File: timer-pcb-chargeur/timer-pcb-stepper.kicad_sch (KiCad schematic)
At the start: 7 parts, among them J11 JST_04, J3 On/off

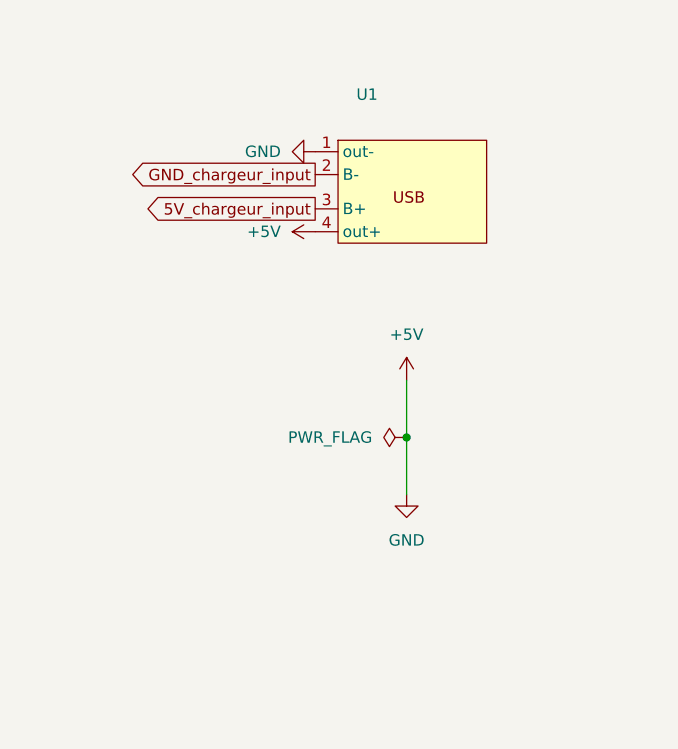
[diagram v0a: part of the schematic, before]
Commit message: mise à jour fichier kicad stepper + led. création dossier chargeur PCB.création du fichier .rpt
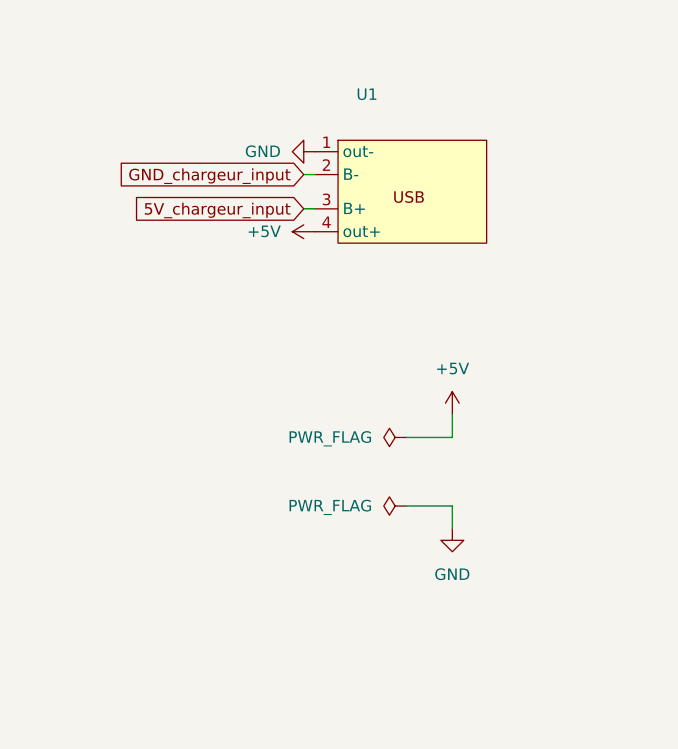
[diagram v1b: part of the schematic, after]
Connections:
- net +5V: no longer J11.1, U1.1 (out-)
- new net GND: J11.1, U1.1 (out-)
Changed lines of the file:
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@@
 		(date "27.05.25")
+	)
+	(rectangle
+		(start 39.37 85.09)
+		(end 39.37 85.09)
+		(stroke
+			(width 0)
+			(type default)
+		)
+		(fill
+			(type none)
+		)
 	)
 	(text "Mounting hole\n"
@@
 		)
 	)
-	(junction
-		(at 54.61 153.67)
-		(diameter 0)
-		(color 0 0 0 0)
-	)
 	(wire
 		(pts
-			(xy 54.61 153.67) (xy 54.61 160.02)
+			(xy 59.69 151.13) (xy 59.69 153.67)
 		)
 		(stroke
@@
 	(wire
 		(pts
-			(xy 54.61 147.32) (xy 54.61 153.67)
+			(xy 43.18 124.46) (xy 44.45 124.46)
 		)
 		(stroke
@@
 			(width 0)
 			(type dash)
+		)
+	)
+	(wire
+		(pts
+			(xy 59.69 153.67) (xy 54.61 153.67)
+		)
+		(stroke
+			(width 0)
+			(type default)
+		)
+	)
+	(wire
+		(pts
+			(xy 43.18 128.27) (xy 44.45 128.27)
+		)
+		(stroke
+			(width 0)
+			(type default)
+		)
+	)
+	(wire
+		(pts
+			(xy 59.69 163.83) (xy 59.69 161.29)
+		)
+		(stroke
+			(width 0)
+			(type default)
+		)
+	)
+	(wire
+		(pts
+			(xy 54.61 161.29) (xy 59.69 161.29)
+		)
+		(stroke
+			(width 0)
+			(type default)
 		)
 	)
@@
 	)
 	(global_label "5V_chargeur_input"
-		(shape output)
-		(at 44.45 128.27 180)
+		(shape input)
+		(at 43.18 128.27 180)
 		(fields_autoplaced yes)
 		(effects
@@
 		)
 		(property "Intersheetrefs" "${INTERSHEET_REFS}"
-			(at 24.1084 128.27 0)
+			(at 22.8384 128.27 0)
 			(effects
 				(font
@@
 	)
 	(global_label "GND_chargeur_input"
-		(shape output)
-		(at 44.45 124.46 180)
+		(shape input)
+		(at 43.18 124.46 180)
 		(fields_autoplaced yes)
 		(effects
@@
 		)
 		(property "Intersheetrefs" "${INTERSHEET_REFS}"
-			(at 22.536 124.46 0)
+			(at 21.266 124.46 0)
 			(effects
 				(font
@@
 				(justify right)
 				(hide yes)
+			)
+		)
+	)
+	(symbol
+		(lib_id "power:PWR_FLAG")
+		(at 54.61 161.29 90)
+		(unit 1)
+		(exclude_from_sim no)
+		(in_bom yes)
+		(on_board yes)
+		(dnp no)
+		(fields_autoplaced yes)
+		(property "Reference" "#FLG02"
+			(at 52.705 161.29 0)
+			(effects
+				(font
+					(size 1.27 1.27)
+				)
+				(hide yes)
+			)
+		)
+		(property "Value" "PWR_FLAG"
+			(at 50.8 161.2899 90)
+			(effects
+				(font
+					(size 1.27 1.27)
+				)
+				(justify left)
+			)
+		)
+		(property "Footprint" ""
+			(at 54.61 161.29 0)
+			(effects
+				(font
+					(size 1.27 1.27)
+				)
+				(hide yes)
+			)
+		)
+		(property "Datasheet" "~"
+			(at 54.61 161.29 0)
+			(effects
+				(font
+					(size 1.27 1.27)
+				)
+				(hide yes)
+			)
+		)
+		(property "Description" "Special symbol for telling ERC where power comes from"
+			(at 54.61 161.29 0)
+			(effects
+				(font
+					(size 1.27 1.27)
+				)
+				(hide yes)
+			)
+		)
+		(pin "1"
+		)
+		(instances
+			(project "timer-pcb-stepper"
+				(path "/c4cfdf40-c3b2-4c58-998c-a7d7b70b9691"
+					(reference "#FLG02")
+					(unit 1)
+				)
 			)
 		)
@@
 	(symbol
 		(lib_id "power:VCC")
-		(at 54.61 147.32 0)
+		(at 59.69 151.13 0)
 		(mirror y)
 		(unit 1)
@@
 		(dnp no)
 		(property "Reference" "#PWR034"
-			(at 54.61 151.13 0)
+			(at 59.69 154.94 0)
 			(effects
 				(font
@@
 		)
 		(property "Value" "+5V"
-			(at 54.61 142.24 0)
+			(at 59.69 146.05 0)
 			(effects
 				(font
@@
 		)
 		(property "Footprint" ""
-			(at 54.61 147.32 0)
+			(at 59.69 151.13 0)
 			(effects
 				(font
@@
 		)
 		(property "Datasheet" ""
-			(at 54.61 147.32 0)
+			(at 59.69 151.13 0)
 			(effects
 				(font
@@
 		)
 		(property "Description" "Power symbol creates a global label with name \"VCC\""
-			(at 54.61 147.32 0)
+			(at 59.69 151.13 0)
 			(effects
 				(font
@@
 	(symbol
 		(lib_id "power:GND")
-		(at 54.61 160.02 0)
+		(at 59.69 163.83 0)
 		(unit 1)
 		(exclude_from_sim no)
@@
 		(fields_autoplaced yes)
 		(property "Reference" "#PWR029"
-			(at 54.61 166.37 0)
+			(at 59.69 170.18 0)
 			(effects
 				(font
@@
 		)
 		(property "Value" "GND"
-			(at 54.61 165.1 0)
+			(at 59.69 168.91 0)
 			(effects
 				(font
@@
 		)
 		(property "Footprint" ""
-			(at 54.61 160.02 0)
+			(at 59.69 163.83 0)
 			(effects
 				(font
@@
 		)
 		(property "Datasheet" ""
-			(at 54.61 160.02 0)
+			(at 59.69 163.83 0)
 			(effects
 				(font
@@
 		)
 		(property "Description" "Power symbol creates a global label with name \"GND\" , ground"
-			(at 54.61 160.02 0)
-			(effects
-				(font
+			(at 59.69 163.83 0)
+			(effects
+				(font
